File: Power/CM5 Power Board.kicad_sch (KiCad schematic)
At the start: 7 parts, among them J1 703W-00_53, J5 691101810005, U1 UWS-5_10-Q48N-C

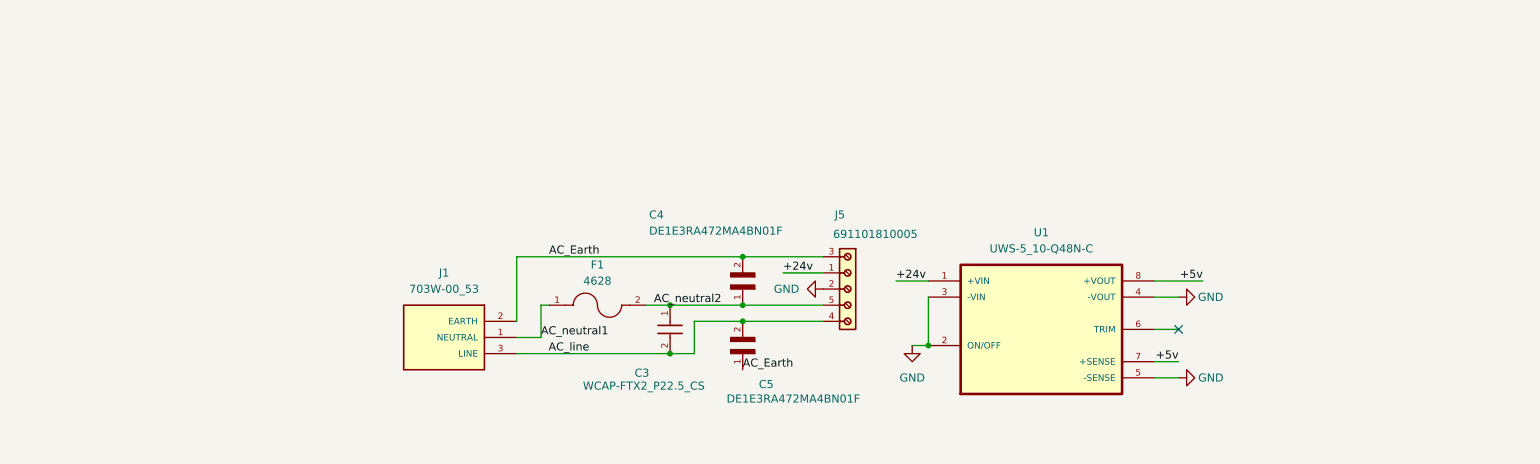
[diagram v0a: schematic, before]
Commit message: adds TX coil half bridge to power board
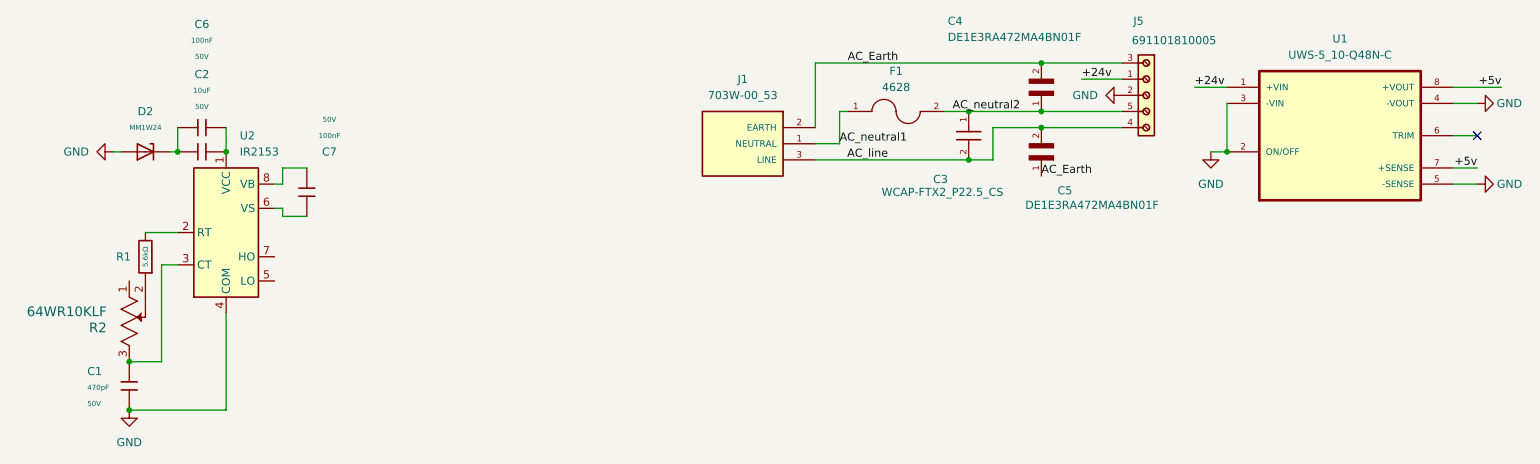
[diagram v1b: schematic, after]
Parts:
- added C1: 470pF, PCM_JLCPCB:C_0805, symbol PCM_JLCPCB-Capacitors:0805,470pF
- added C2: 10uF, PCM_JLCPCB:C_1206, symbol PCM_JLCPCB-Capacitors:1206,10uF
- added C6, C7: 100nF, PCM_JLCPCB:C_0603, symbol PCM_JLCPCB-Capacitors:0603,100nF
- added D2: MM1W24, PCM_JLCPCB:D_SOD-123, symbol PCM_JLCPCB-Diodes:Zener,MM1W24
- added R1: 5.6kΩ, PCM_JLCPCB:R_0805, symbol PCM_JLCPCB-Resistors:0805,5.6kΩ
- added R2: 64WR10KLF, Custom Components:RES3_64W_TTE, symbol RES3_64W_TTE:64WR10KLF
- added U2: IR2153, symbol Driver_FET:IR2153
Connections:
- net GND: now also C1.2, D2.2, U2.4 (COM)
- new net: C7.1, U2.6 (VS)
- new net: C7.2, U2.8 (VB)
- new net: C2.1, C6.1, D2.1
- new net: C2.2, C6.2, U2.1 (VCC)
- new net: C1.1, R2.3, U2.3 (CT)
- new net: R1.2, U2.2 (RT)
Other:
- moved on the sheet: C3, C4, C5, F1, J1, J5, U1

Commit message: corrects power board for 400W max power production at 24v and 5v rail
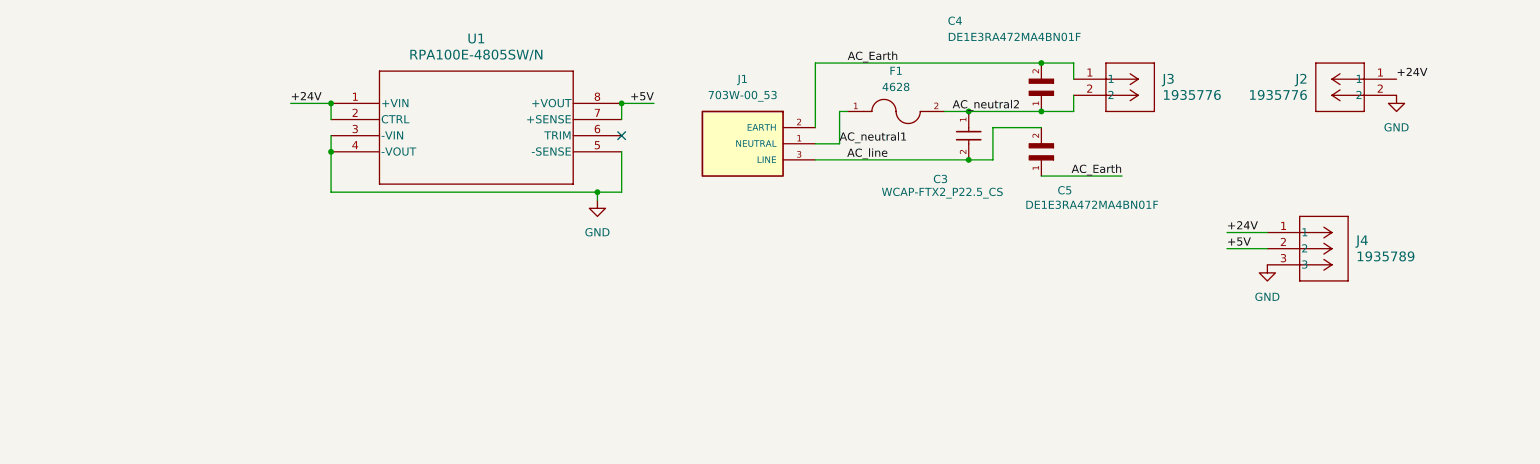
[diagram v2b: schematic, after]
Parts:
- removed C1: 470pF, PCM_JLCPCB:C_0805, symbol PCM_JLCPCB-Capacitors:0805,470pF
- removed C2: 10uF, PCM_JLCPCB:C_1206, symbol PCM_JLCPCB-Capacitors:1206,10uF
- removed C6, C7: 100nF, PCM_JLCPCB:C_0603, symbol PCM_JLCPCB-Capacitors:0603,100nF
- removed D2: MM1W24, PCM_JLCPCB:D_SOD-123, symbol PCM_JLCPCB-Diodes:Zener,MM1W24
- removed J5: 691101810005, Custom Components:691101810005, symbol 691101810005:691101810005
- removed R1: 5.6kΩ, PCM_JLCPCB:R_0805, symbol PCM_JLCPCB-Resistors:0805,5.6kΩ
- removed R2: 64WR10KLF, Custom Components:RES3_64W_TTE, symbol RES3_64W_TTE:64WR10KLF
- removed U1: UWS-5_10-Q48N-C, Custom Components:VREG_UWS-5_10-Q48N-C, symbol UWS-5_10-Q48N-C:UWS-5_10-Q48N-C
- removed U2: IR2153, symbol Driver_FET:IR2153
- added J2, J3: 1935776, Custom Components:CONN_1935776_PXC, symbol CONN_1935776_PX:1935776
- added J4: 1935789, Custom Components:CONN_1935789_PXC, symbol CONN_1935789_PXC:1935789
- added U1: RPA100E-4805SW/N, Custom Components:RPA100E-W_RCP, symbol RPA100E-W_RCP:RPA100E-4805SW_N
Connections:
- net AC_Earth: now also J3.1
- net AC_neutral2: now also J3.2
- net GND: now also J2.2, J4.3, U1.3 (-VIN), U1.4 (-VOUT), U1.5 (-SENSE)
- new net +24V: J2.1, J4.1, U1.1 (+VIN), U1.2 (CTRL)
- new net +5V: J4.2, U1.7 (+SENSE), U1.8 (+VOUT)
